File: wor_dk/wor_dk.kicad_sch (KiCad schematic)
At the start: 9 parts, among them J101 Conn_01x02, J102 Conn_02x03_Odd_Even, J103 Conn_02x03_Odd_Even, J104 Conn_01x02

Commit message: wor_dk: add footprints & part info for all resistors
All resistors are JLCPCB basic parts. Footprint 0402 is used for all
resistors, except for 0 Ω resistors, where 0805 is used.
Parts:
- R101: MPN (none) -> 0402WGF2201TCE
- R102, R103, R104: footprint (none) -> Resistor_SMD:R_0805_2012Metric; Comment (none) -> JLCPCB basic part; LCSC (none) -> C17477; MPN (none) -> 0805W8F0000T5E; Manufacturer (none) -> Uniroyal Elec
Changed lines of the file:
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@@
 			)
 		)
-		(property "Footprint" ""
+		(property "Footprint" "Resistor_SMD:R_0805_2012Metric"
 			(at 156.21 127.762 90)
 			(effects
@@
 			)
 		)
-		(property "Datasheet" "~"
+		(property "Datasheet" "https://wmsc.lcsc.com/wmsc/upload/file/pdf/v2/lcsc/2206010216_UNI-ROYAL-Uniroyal-Elec-0805W8F0000T5E_C17477.pdf"
 			(at 156.21 129.54 0)
 			(effects
@@
 			)
 		)
-		(property "Description" "Resistor"
+		(property "Description" "25mW Thick Film Resistors 150V ±800ppm/℃ ±1% 0Ω 0805"
+			(at 156.21 129.54 0)
+			(effects
+				(font
+					(size 1.27 1.27)
+				)
+				(hide yes)
+			)
+		)
+		(property "Comment" "JLCPCB basic part"
+			(at 156.21 129.54 0)
+			(effects
+				(font
+					(size 1.27 1.27)
+				)
+				(hide yes)
+			)
+		)
+		(property "LCSC" "C17477"
+			(at 156.21 129.54 0)
+			(effects
+				(font
+					(size 1.27 1.27)
+				)
+				(hide yes)
+			)
+		)
+		(property "MPN" "0805W8F0000T5E"
+			(at 156.21 129.54 0)
+			(effects
+				(font
+					(size 1.27 1.27)
+				)
+				(hide yes)
+			)
+		)
+		(property "Manufacturer" "Uniroyal Elec"
 			(at 156.21 129.54 0)
 			(effects
@@
 			)
 		)
-		(property "Footprint" ""
+		(property "Footprint" "Resistor_SMD:R_0805_2012Metric"
 			(at 156.21 122.682 90)
 			(effects
@@
 			)
 		)
-		(property "Datasheet" "~"
+		(property "Datasheet" "https://wmsc.lcsc.com/wmsc/upload/file/pdf/v2/lcsc/2206010216_UNI-ROYAL-Uniroyal-Elec-0805W8F0000T5E_C17477.pdf"
 			(at 156.21 124.46 0)
 			(effects
@@
 			)
 		)
-		(property "Description" "Resistor"
+		(property "Description" "25mW Thick Film Resistors 150V ±800ppm/℃ ±1% 0Ω 0805"
+			(at 156.21 124.46 0)
+			(effects
+				(font
+					(size 1.27 1.27)
+				)
+				(hide yes)
+			)
+		)
+		(property "Comment" "JLCPCB basic part"
+			(at 156.21 124.46 0)
+			(effects
+				(font
+					(size 1.27 1.27)
+				)
+				(hide yes)
+			)
+		)
+		(property "LCSC" "C17477"
+			(at 156.21 124.46 0)
+			(effects
+				(font
+					(size 1.27 1.27)
+				)
+				(hide yes)
+			)
+		)
+		(property "MPN" "0805W8F0000T5E"
+			(at 156.21 124.46 0)
+			(effects
+				(font
+					(size 1.27 1.27)
+				)
+				(hide yes)
+			)
+		)
+		(property "Manufacturer" "Uniroyal Elec"
 			(at 156.21 124.46 0)
 			(effects
@@
 			)
 		)
-		(property "Footprint" ""
+		(property "Footprint" "Resistor_SMD:R_0805_2012Metric"
 			(at 156.21 125.222 90)
 			(effects
@@
 			)
 		)
-		(property "Datasheet" "~"
+		(property "Datasheet" "https://wmsc.lcsc.com/wmsc/upload/file/pdf/v2/lcsc/2206010216_UNI-ROYAL-Uniroyal-Elec-0805W8F0000T5E_C17477.pdf"
 			(at 156.21 127 0)
 			(effects
@@
 			)
 		)
-		(property "Description" "Resistor"
+		(property "Description" "25mW Thick Film Resistors 150V ±800ppm/℃ ±1% 0Ω 0805"
+			(at 156.21 127 0)
+			(effects
+				(font
+					(size 1.27 1.27)
+				)
+				(hide yes)
+			)
+		)
+		(property "Comment" "JLCPCB basic part"
+			(at 156.21 127 0)
+			(effects
+				(font
+					(size 1.27 1.27)
+				)
+				(hide yes)
+			)
+		)
+		(property "LCSC" "C17477"
+			(at 156.21 127 0)
+			(effects
+				(font
+					(size 1.27 1.27)
+				)
+				(hide yes)
+			)
+		)
+		(property "MPN" "0805W8F0000T5E"
+			(at 156.21 127 0)
+			(effects
+				(font
+					(size 1.27 1.27)
+				)
+				(hide yes)
+			)
+		)
+		(property "Manufacturer" "Uniroyal Elec"
 			(at 156.21 127 0)
 			(effects
@@
 			(at 38.1 142.24 0)
 			(effects
+				(font
+					(size 1.27 1.27)
+				)
+				(hide yes)
+			)
+		)
+		(property "MPN" "0402WGF2201TCE"
+			(at 38.1 142.24 0)
+			(effects

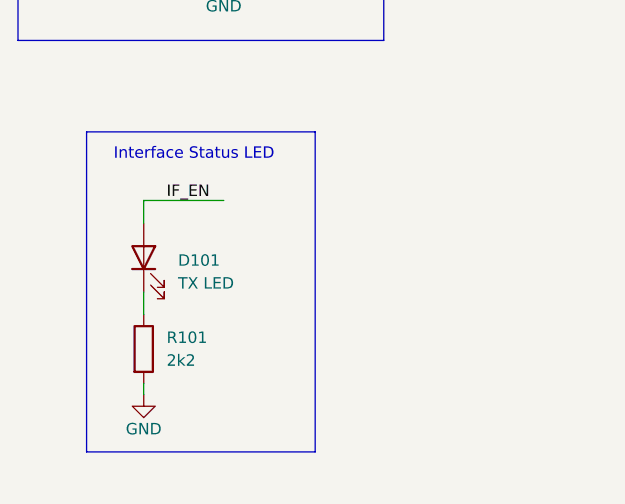
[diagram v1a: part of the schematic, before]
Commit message: wor_dk: add footprints & part info for all diodes & LEDs
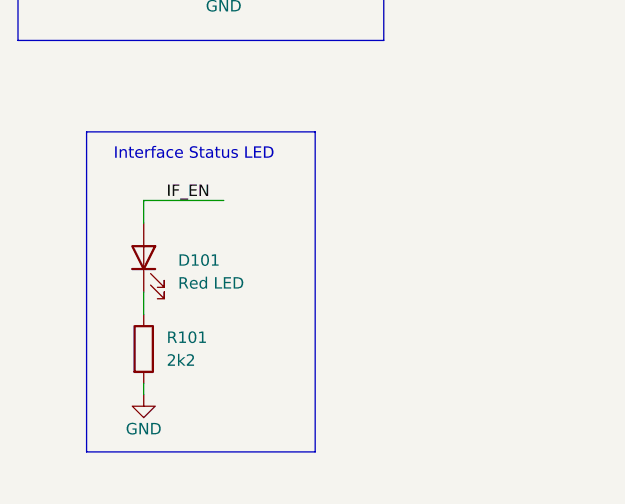
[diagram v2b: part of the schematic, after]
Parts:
- D101: value TX LED -> Red LED; Comment JLCPCB basic part -> Interface active LED; JLCPCB basic part; MPN (none) -> NCD0805R1
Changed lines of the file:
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@@
 			)
 		)
-		(property "Value" "TX LED"
+		(property "Value" "Red LED"
 			(at 41.91 134.9374 90)
 			(effects
@@
 			)
 		)
-		(property "Description" "Red 0805 Light Emitting Diodes (LED) ROHS"
+		(property "Description" "25mA Colorless transparent lens 67mcd~195mcd -30℃~+85℃ 615nm~630nm Individual diode Red 130° 65mW 1.6V~2.6V 0805 LED Indication - Discrete ROHS"
 			(at 38.1 132.08 0)
 			(effects
@@
 			)
 		)
-		(property "Comment" "JLCPCB basic part"
+		(property "Comment" "Interface active LED; JLCPCB basic part"
 			(at 38.1 132.08 0)
 			(effects
@@
 			(at 38.1 132.08 0)
 			(effects
+				(font
+					(size 1.27 1.27)
+				)
+				(hide yes)
+			)
+		)
+		(property "MPN" "NCD0805R1"
+			(at 38.1 132.08 0)
+			(effects

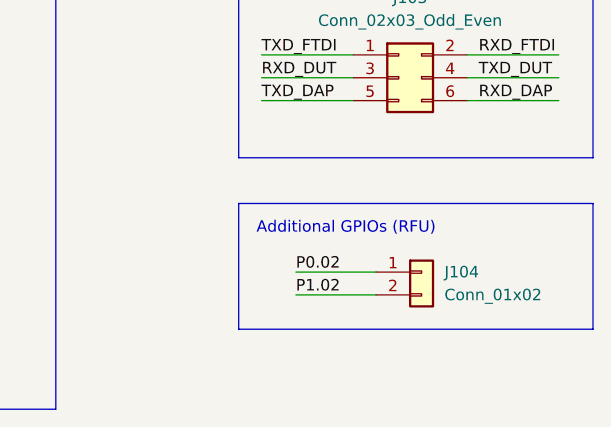
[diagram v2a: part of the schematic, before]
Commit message: wor_dk: add all footprints & part info for connectors
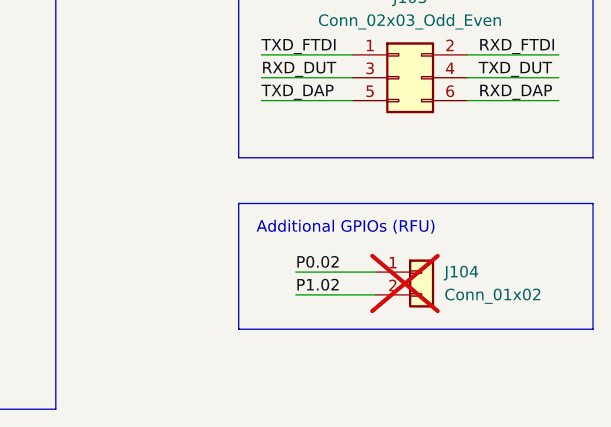
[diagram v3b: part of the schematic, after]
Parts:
- J101: footprint (none) -> Connector_PinHeader_2.54mm:PinHeader_1x02_P2.54mm_Horizontal; LCSC (none) -> C492410; MPN (none) -> PZ254R-11-02P; Manufacturer (none) -> XFCN
- J102, J103: footprint (none) -> Connector_PinHeader_2.54mm:PinHeader_2x03_P2.54mm_Vertical; LCSC (none) -> C65114; MPN (none) -> 2.54-2*3P; Manufacturer (none) -> Boom Precision Elec
- J104: footprint (none) -> Connector_PinHeader_2.54mm:PinHeader_1x02_P2.54mm_Vertical; LCSC (none) -> C2905434; MPN (none) -> KH-2.54PH180-1X2P-L11.5; Manufacturer (none) -> Shenzhen Kinghelm Elec; now not fitted
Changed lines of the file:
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@@
 			)
 		)
-		(property "Footprint" ""
+		(property "Footprint" "Connector_PinHeader_2.54mm:PinHeader_2x03_P2.54mm_Vertical"
 			(at 234.95 120.65 0)
 			(effects
@@
 			)
 		)
-		(property "Datasheet" "~"
+		(property "Datasheet" "https://jlcpcb.com/partdetail/boomele_boom_Precision_elec-2_54_23P/C65114"
 			(at 234.95 120.65 0)
 			(effects
@@
 		)
 		(property "Description" "Generic connector, double row, 02x03, odd/even pin numbering scheme (row 1 odd numbers, row 2 even numbers), script generated (kicad-library-utils/schlib/autogen/connector/)"
+			(at 234.95 120.65 0)
+			(effects
+				(font
+					(size 1.27 1.27)
+				)
+				(hide yes)
+			)
+		)
+		(property "LCSC" "C65114"
+			(at 234.95 120.65 0)
+			(effects
+				(font
+					(size 1.27 1.27)
+				)
+				(hide yes)
+			)
+		)
+		(property "MPN" "2.54-2*3P"
+			(at 234.95 120.65 0)
+			(effects
+				(font
+					(size 1.27 1.27)
+				)
+				(hide yes)
+			)
+		)
+		(property "Manufacturer" "Boom Precision Elec"
 			(at 234.95 120.65 0)
 			(effects
@@
 			)
 		)
-		(property "Footprint" ""
+		(property "Footprint" "Connector_PinHeader_2.54mm:PinHeader_1x02_P2.54mm_Horizontal"
 			(at 40.64 96.52 0)
 			(effects
@@
 			)
 		)
-		(property "Datasheet" "~"
+		(property "Datasheet" "https://wmsc.lcsc.com/wmsc/upload/file/pdf/v2/lcsc/2003191006_XFCN-PZ254R-11-02P_C492410.pdf"
 			(at 40.64 96.52 0)
 			(effects
@@
 		)
 		(property "Description" "Generic connector, single row, 01x02, script generated (kicad-library-utils/schlib/autogen/connector/)"
+			(at 40.64 96.52 0)
+			(effects
+				(font
+					(size 1.27 1.27)
+				)
+				(hide yes)
+			)
+		)
+		(property "LCSC" "C492410"
+			(at 40.64 96.52 0)
+			(effects
+				(font
+					(size 1.27 1.27)
+				)
+				(hide yes)
+			)
+		)
+		(property "MPN" "PZ254R-11-02P"
+			(at 40.64 96.52 0)
+			(effects
+				(font
+					(size 1.27 1.27)
+				)
+				(hide yes)
+			)
+		)
+		(property "Manufacturer" "XFCN"
 			(at 40.64 96.52 0)
 			(effects
@@
 			)
 		)
-		(property "Footprint" ""
+		(property "Footprint" "Connector_PinHeader_2.54mm:PinHeader_2x03_P2.54mm_Vertical"
 			(at 234.95 95.25 0)
 			(effects
@@
 			)
 		)
-		(property "Datasheet" "~"
+		(property "Datasheet" "https://jlcpcb.com/partdetail/boomele_boom_Precision_elec-2_54_23P/C65114"
 			(at 234.95 95.25 0)
 			(effects
@@
 		)
 		(property "Description" "Generic connector, double row, 02x03, odd/even pin numbering scheme (row 1 odd numbers, row 2 even numbers), script generated (kicad-library-utils/schlib/autogen/connector/)"
+			(at 234.95 95.25 0)
+			(effects
+				(font
+					(size 1.27 1.27)
+				)
+				(hide yes)
+			)
+		)
+		(property "LCSC" "C65114"
+			(at 234.95 95.25 0)
+			(effects
+				(font
+					(size 1.27 1.27)
+				)
+				(hide yes)
+			)
+		)
+		(property "MPN" "2.54-2*3P"
+			(at 234.95 95.25 0)
+			(effects
+				(font
+					(size 1.27 1.27)
+				)
+				(hide yes)
+			)
+		)
+		(property "Manufacturer" "Boom Precision Elec"
 			(at 234.95 95.25 0)
 			(effects
@@
 		(in_bom yes)
 		(on_board yes)
-		(dnp no)
+		(dnp yes)
 		(fields_autoplaced yes)
 		(property "Reference" "J104"
@@
 			)
 		)
-		(property "Footprint" ""
+		(property "Footprint" "Connector_PinHeader_2.54mm:PinHeader_1x02_P2.54mm_Vertical"
 			(at 237.49 142.24 0)
 			(effects
@@
 			)
 		)
-		(property "Datasheet" "~"
+		(property "Datasheet" "https://wmsc.lcsc.com/wmsc/upload/file/pdf/v2/lcsc/2110191530_Shenzhen-Kinghelm-Elec-KH-2-54PH180-1X2P-L11-5_C2905434.pdf"
 			(at 237.49 142.24 0)
 			(effects
@@
 			(at 237.49 142.24 0)
 			(effects
+				(font
+					(size 1.27 1.27)
+				)
+				(hide yes)
+			)
+		)
+		(property "LCSC" "C2905434"
+			(at 237.49 142.24 0)
+			(effects
+				(font
+					(size 1.27 1.27)
+				)
+				(hide yes)
+			)
+		)
+		(property "MPN" "KH-2.54PH180-1X2P-L11.5"
+			(at 237.49 142.24 0)
+			(effects
+				(font
+					(size 1.27 1.27)
+				)
+				(hide yes)
+			)
+		)
+		(property "Manufacturer" "Shenzhen Kinghelm Elec"
+			(at 237.49 142.24 0)
+			(effects

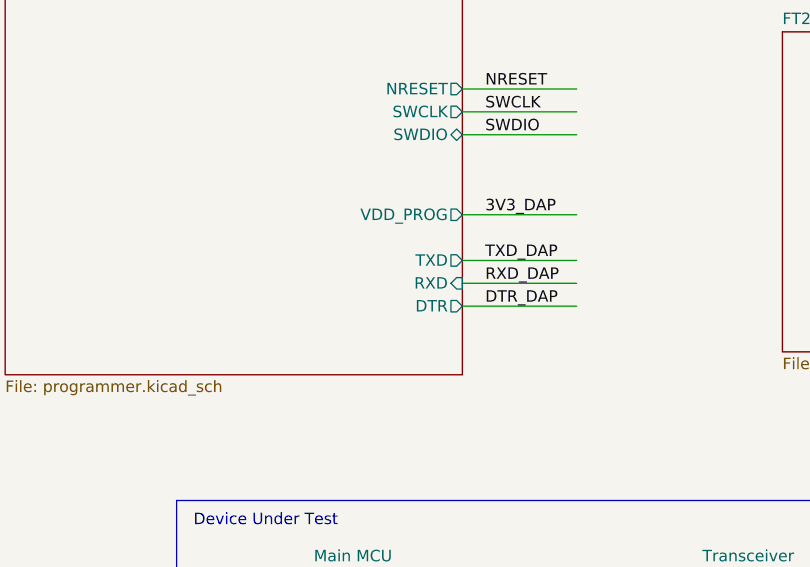
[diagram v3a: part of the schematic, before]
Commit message: wor_dk: schematic: fix LPC11U35 pins
The following signals of the LPC11U35 DAPLink were accidentally
connected due to identical labels on both sides:
- RXD across R507
- TXD across R509
- DTR across R510
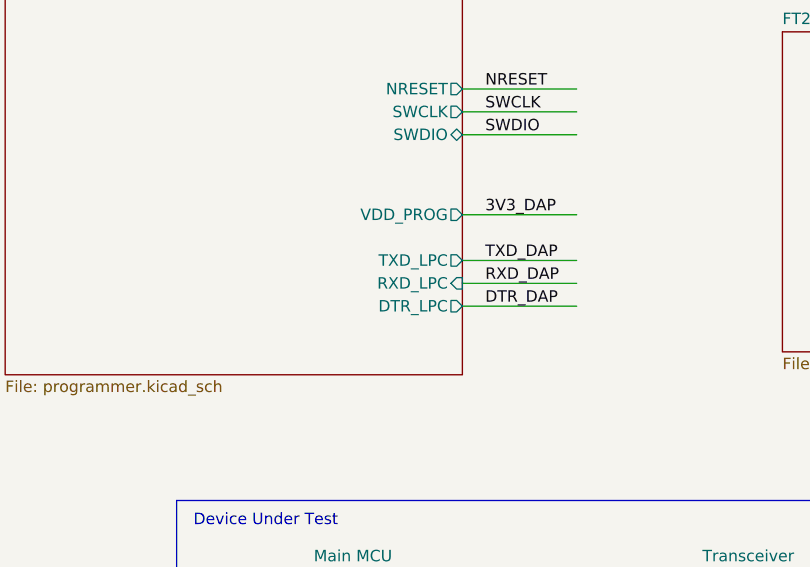
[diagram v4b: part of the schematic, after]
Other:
- sheet LPC11U35 DAPLink Programmer ports: added DTR_LPC, RXD_LPC, TXD_LPC; removed DTR, RXD, TXD
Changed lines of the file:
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@@
-			)
-		)
-		(pin "DTR" output
-			(at 127 55.88 0)
-			(effects
-				(font
-					(size 1.27 1.27)
-				)
-				(justify right)
 			)
 		)
 		(pin "SWDIO" bidirectional
 			(at 127 36.83 0)
-			(effects
-				(font
-					(size 1.27 1.27)
-				)
-				(justify right)
-			)
-		)
-		(pin "TXD" output
-			(at 127 50.8 0)
-			(effects
-				(font
-					(size 1.27 1.27)
-				)
-				(justify right)
-			)
-		)
-		(pin "RXD" input
-			(at 127 53.34 0)
 			(effects
 				(font
@@
 			(effects
 				(font
+					(size 1.27 1.27)
+				)
+				(justify right)
+			)
+		)
+		(pin "TXD_LPC" output
+			(at 127 50.8 0)
+			(effects
+				(font
+					(size 1.27 1.27)
+				)
+				(justify right)
+			)
+		)
+		(pin "DTR_LPC" output
+			(at 127 55.88 0)
+			(effects
+				(font
+					(size 1.27 1.27)
+				)
+				(justify right)
+			)
+		)
+		(pin "RXD_LPC" input
+			(at 127 53.34 0)
+			(effects
+				(font

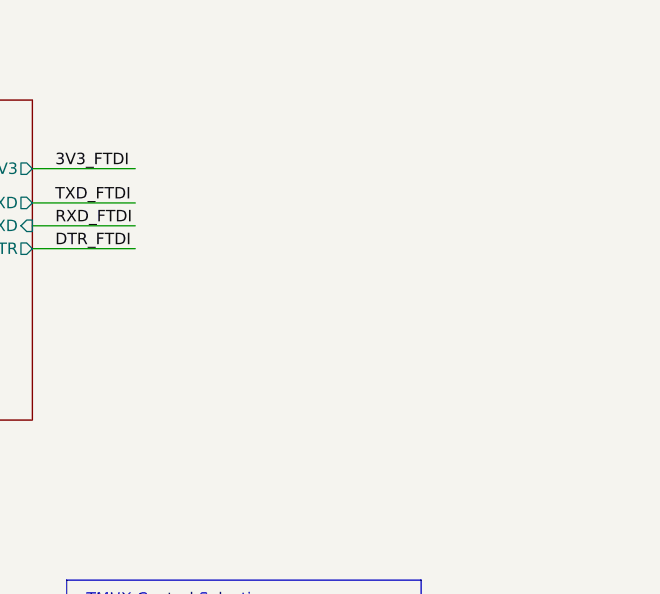
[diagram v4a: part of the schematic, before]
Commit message: wor_dk: add M2.5 screw holes
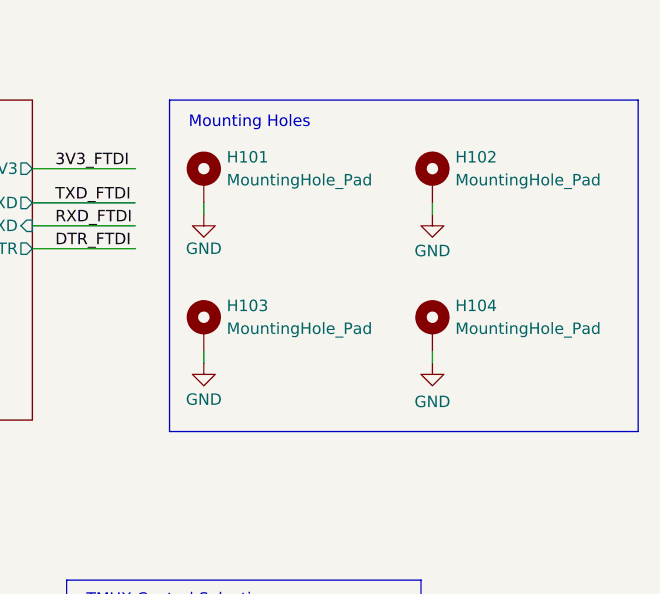
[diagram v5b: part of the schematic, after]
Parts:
- added H101, H102, H103, H104: MountingHole_Pad, MountingHole:MountingHole_2.7mm_M2.5_ISO7380_Pad, symbol Mechanical:MountingHole_Pad
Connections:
- net GND: now also H101.1, H102.1, H103.1, H104.1
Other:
- note added: "Mounting Holes"
